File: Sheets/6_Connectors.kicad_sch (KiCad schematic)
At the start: 2 parts, among them J4 Conn_02x26_Odd_Even, J5 Conn_02x26_Odd_Even

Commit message: Updates for revision 2
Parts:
- J4, J5: MANUFACTURER (none) -> HRS(Hirose); MAXIMUM_PACKAGE_HEIGHT HRS(Hirose) -> (none)
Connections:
- net VCC is gone; now on net +3V3: J4.51 (Pin_51), J4.52 (Pin_52)
- net P1.09 renamed P1.09/~{CHARGE}

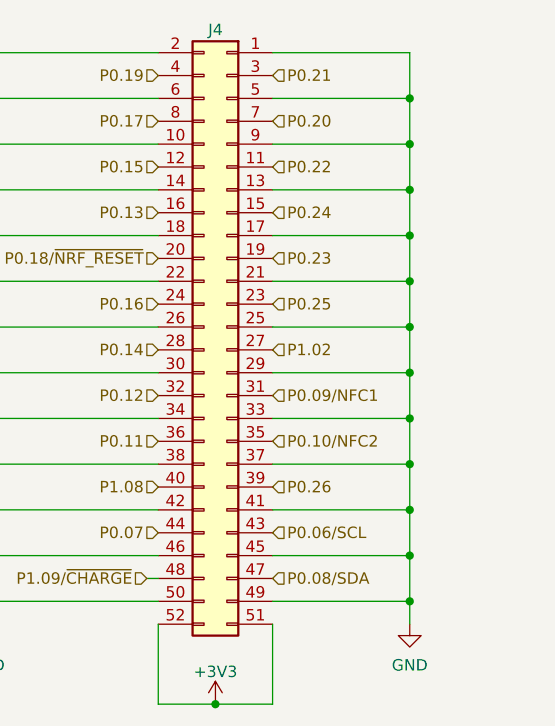
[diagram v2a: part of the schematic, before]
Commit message: Moving some tracks and increasing via diameter to allow for latest JLCPCB capabilities
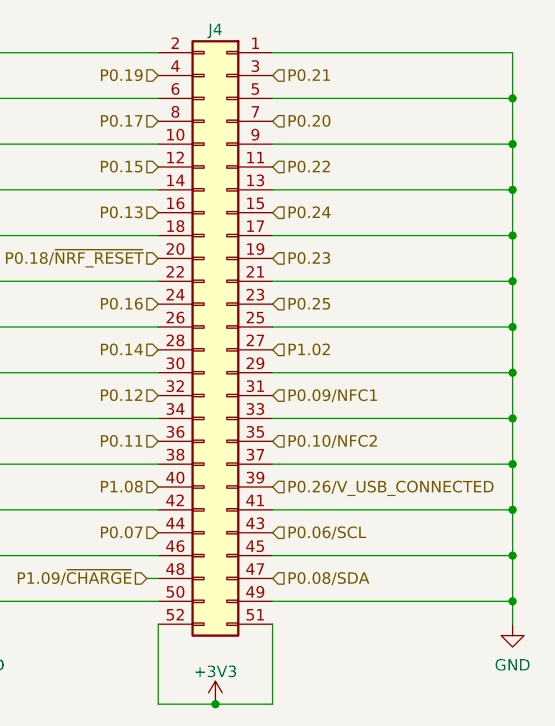
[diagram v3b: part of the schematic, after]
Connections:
- net P0.26 renamed P0.26/V_USB_CONNECTED
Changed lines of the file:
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@@
   (junction (at 158.75 64.77) (diameter 0) (color 0 0 0 0)
   )
-  (junction (at 205.74 59.69) (diameter 0) (color 0 0 0 0)
+  (junction (at 217.17 59.69) (diameter 0) (color 0 0 0 0)
   )
   (junction (at 72.39 71.12) (diameter 0) (color 0 0 0 0)
@@
   (junction (at 158.75 85.09) (diameter 0) (color 0 0 0 0)
   )
-  (junction (at 205.74 85.09) (diameter 0) (color 0 0 0 0)
-  )
-  (junction (at 205.74 100.33) (diameter 0) (color 0 0 0 0)
+  (junction (at 217.17 85.09) (diameter 0) (color 0 0 0 0)
   )
   (junction (at 113.03 88.9) (diameter 0) (color 0 0 0 0)
@@
   (junction (at 158.75 59.69) (diameter 0) (color 0 0 0 0)
   )
-  (junction (at 205.74 110.49) (diameter 0) (color 0 0 0 0)
+  (junction (at 217.17 110.49) (diameter 0) (color 0 0 0 0)
   )
   (junction (at 72.39 81.28) (diameter 0) (color 0 0 0 0)
@@
   (junction (at 113.03 101.6) (diameter 0) (color 0 0 0 0)
   )
-  (junction (at 205.74 74.93) (diameter 0) (color 0 0 0 0)
+  (junction (at 217.17 74.93) (diameter 0) (color 0 0 0 0)
   )
   (junction (at 113.03 96.52) (diameter 0) (color 0 0 0 0)
   )
+  (junction (at 217.17 100.33) (diameter 0) (color 0 0 0 0)
+  )
   (junction (at 113.03 60.96) (diameter 0) (color 0 0 0 0)
   )
@@
   (junction (at 113.03 116.84) (diameter 0) (color 0 0 0 0)
   )
+  (junction (at 217.17 105.41) (diameter 0) (color 0 0 0 0)
+  )
   (junction (at 184.15 127) (diameter 0) (color 0 0 0 0)
   )
   (junction (at 158.75 100.33) (diameter 0) (color 0 0 0 0)
   )
-  (junction (at 205.74 64.77) (diameter 0) (color 0 0 0 0)
+  (junction (at 217.17 64.77) (diameter 0) (color 0 0 0 0)
   )
   (junction (at 158.75 105.41) (diameter 0) (color 0 0 0 0)
@@
   (junction (at 113.03 81.28) (diameter 0) (color 0 0 0 0)
   )
-  (junction (at 205.74 105.41) (diameter 0) (color 0 0 0 0)
-  )
   (junction (at 113.03 76.2) (diameter 0) (color 0 0 0 0)
   )
@@
   (junction (at 72.39 111.76) (diameter 0) (color 0 0 0 0)
   )
-  (junction (at 205.74 95.25) (diameter 0) (color 0 0 0 0)
+  (junction (at 217.17 95.25) (diameter 0) (color 0 0 0 0)
   )
   (junction (at 72.39 76.2) (diameter 0) (color 0 0 0 0)
@@
   (junction (at 72.39 86.36) (diameter 0) (color 0 0 0 0)
   )
-  (junction (at 205.74 69.85) (diameter 0) (color 0 0 0 0)
-  )
-  (junction (at 205.74 90.17) (diameter 0) (color 0 0 0 0)
+  (junction (at 217.17 69.85) (diameter 0) (color 0 0 0 0)
+  )
+  (junction (at 217.17 90.17) (diameter 0) (color 0 0 0 0)
   )
   (junction (at 158.75 74.93) (diameter 0) (color 0 0 0 0)
@@
   (junction (at 113.03 66.04) (diameter 0) (color 0 0 0 0)
   )
-  (junction (at 205.74 80.01) (diameter 0) (color 0 0 0 0)
+  (junction (at 217.17 80.01) (diameter 0) (color 0 0 0 0)
   )
   (junction (at 113.03 111.76) (diameter 0) (color 0 0 0 0)
@@
   (junction (at 72.39 96.52) (diameter 0) (color 0 0 0 0)
   )
-  (junction (at 205.74 115.57) (diameter 0) (color 0 0 0 0)
+  (junction (at 217.17 115.57) (diameter 0) (color 0 0 0 0)
   )
   (wire (pts (xy 158.75 100.33) (xy 158.75 105.41))
@@
     (stroke (width 0) (type default))
   )
-  (wire (pts (xy 205.74 69.85) (xy 205.74 74.93))
+  (wire (pts (xy 217.17 69.85) (xy 217.17 74.93))
     (stroke (width 0) (type default))
   )
@@
     (stroke (width 0) (type default))
   )
-  (wire (pts (xy 190.5 69.85) (xy 205.74 69.85))
+  (wire (pts (xy 190.5 69.85) (xy 217.17 69.85))
     (stroke (width 0) (type default))
   )
@@
     (stroke (width 0) (type default))
   )
-  (wire (pts (xy 190.5 80.01) (xy 205.74 80.01))
+  (wire (pts (xy 190.5 80.01) (xy 217.17 80.01))
     (stroke (width 0) (type default))
   )
@@
     (stroke (width 0) (type default))
   )
+  (wire (pts (xy 190.5 110.49) (xy 217.17 110.49))
+    (stroke (width 0) (type default))
+  )
   (wire (pts (xy 158.75 105.41) (xy 177.8 105.41))
     (stroke (width 0) (type default))
@@
     (stroke (width 0) (type default))
   )
-  (wire (pts (xy 205.74 90.17) (xy 190.5 90.17))
-    (stroke (width 0) (type default))
-  )
-  (wire (pts (xy 205.74 64.77) (xy 205.74 69.85))
+  (wire (pts (xy 217.17 90.17) (xy 190.5 90.17))
+    (stroke (width 0) (type default))
+  )
+  (wire (pts (xy 217.17 64.77) (xy 217.17 69.85))
     (stroke (width 0) (type default))
   )
@@
     (stroke (width 0) (type default))
   )
-  (wire (pts (xy 190.5 74.93) (xy 205.74 74.93))
+  (wire (pts (xy 190.5 74.93) (xy 217.17 74.93))
     (stroke (width 0) (type default))
   )
@@
     (stroke (width 0) (type default))
   )
+  (wire (pts (xy 190.5 100.33) (xy 217.17 100.33))
+    (stroke (width 0) (type default))
+  )
   (wire (pts (xy 99.06 96.52) (xy 113.03 96.52))
     (stroke (width 0) (type default))
@@
     (stroke (width 0) (type default))
   )
-  (wire (pts (xy 205.74 105.41) (xy 205.74 110.49))
+  (wire (pts (xy 217.17 105.41) (xy 217.17 110.49))
     (stroke (width 0) (type default))
   )
@@
     (stroke (width 0) (type default))
   )
-  (wire (pts (xy 205.74 74.93) (xy 205.74 80.01))
-    (stroke (width 0) (type default))
-  )
-  (wire (pts (xy 190.5 100.33) (xy 205.74 100.33))
+  (wire (pts (xy 217.17 74.93) (xy 217.17 80.01))
     (stroke (width 0) (type default))
   )
@@
     (stroke (width 0) (type default))
   )
-  (wire (pts (xy 205.74 90.17) (xy 205.74 95.25))
+  (wire (pts (xy 217.17 90.17) (xy 217.17 95.25))
     (stroke (width 0) (type default))
   )
@@
     (stroke (width 0) (type default))
   )
-  (wire (pts (xy 190.5 110.49) (xy 205.74 110.49))
-    (stroke (width 0) (type default))
-  )
-  (wire (pts (xy 190.5 54.61) (xy 205.74 54.61))
+  (wire (pts (xy 190.5 54.61) (xy 217.17 54.61))
     (stroke (width 0) (type default))
   )
@@
     (stroke (width 0) (type default))
   )
-  (wire (pts (xy 190.5 59.69) (xy 205.74 59.69))
+  (wire (pts (xy 190.5 59.69) (xy 217.17 59.69))
     (stroke (width 0) (type default))
   )
@@
     (stroke (width 0) (type default))
   )
-  (wire (pts (xy 205.74 54.61) (xy 205.74 59.69))
-    (stroke (width 0) (type default))
-  )
-  (wire (pts (xy 205.74 110.49) (xy 205.74 115.57))
+  (wire (pts (xy 217.17 54.61) (xy 217.17 59.69))
+    (stroke (width 0) (type default))
+  )
+  (wire (pts (xy 217.17 110.49) (xy 217.17 115.57))
     (stroke (width 0) (type default))
   )
@@
     (stroke (width 0) (type default))
   )
-  (wire (pts (xy 205.74 80.01) (xy 205.74 85.09))
+  (wire (pts (xy 217.17 80.01) (xy 217.17 85.09))
     (stroke (width 0) (type default))
   )
@@
     (stroke (width 0) (type default))
   )
-  (wire (pts (xy 205.74 85.09) (xy 205.74 90.17))
+  (wire (pts (xy 217.17 85.09) (xy 217.17 90.17))
     (stroke (width 0) (type default))
   )
@@
     (stroke (width 0) (type default))
   )
-  (wire (pts (xy 190.5 64.77) (xy 205.74 64.77))
+  (wire (pts (xy 190.5 64.77) (xy 217.17 64.77))
     (stroke (width 0) (type default))
   )
@@
     (stroke (width 0) (type default))
   )
-  (wire (pts (xy 205.74 59.69) (xy 205.74 64.77))
+  (wire (pts (xy 217.17 59.69) (xy 217.17 64.77))
     (stroke (width 0) (type default))
   )
@@
     (stroke (width 0) (type default))
   )
-  (wire (pts (xy 205.74 95.25) (xy 205.74 100.33))
+  (wire (pts (xy 217.17 95.25) (xy 217.17 100.33))
     (stroke (width 0) (type default))
   )
@@
     (stroke (width 0) (type default))
   )
-  (wire (pts (xy 205.74 100.33) (xy 205.74 105.41))
+  (wire (pts (xy 217.17 100.33) (xy 217.17 105.41))
     (stroke (width 0) (type default))
   )
@@
     (stroke (width 0) (type default))
   )
-  (wire (pts (xy 190.5 95.25) (xy 205.74 95.25))
+  (wire (pts (xy 190.5 95.25) (xy 217.17 95.25))
     (stroke (width 0) (type default))
   )
@@
     (stroke (width 0) (type default))
   )
-  (wire (pts (xy 205.74 115.57) (xy 205.74 118.11))
+  (wire (pts (xy 217.17 115.57) (xy 217.17 118.11))
     (stroke (width 0) (type default))
   )
@@
     (stroke (width 0) (type default))
   )
-  (wire (pts (xy 190.5 85.09) (xy 205.74 85.09))
+  (wire (pts (xy 190.5 85.09) (xy 217.17 85.09))
     (stroke (width 0) (type default))
   )
@@
     (stroke (width 0) (type default))
   )
-  (wire (pts (xy 190.5 105.41) (xy 205.74 105.41))
-    (stroke (width 0) (type default))
-  )
-  (wire (pts (xy 190.5 115.57) (xy 205.74 115.57))
+  (wire (pts (xy 190.5 105.41) (xy 217.17 105.41))
+    (stroke (width 0) (type default))
+  )
+  (wire (pts (xy 190.5 115.57) (xy 217.17 115.57))
     (stroke (width 0) (type default))
   )
@@
     (effects (font (size 1.27 1.27)) (justify right))
   )
-  (hierarchical_label "P0.26" (shape input) (at 190.5 102.87 0) (fields_autoplaced)
+  (hierarchical_label "P0.26{slash}V_USB_CONNECTED" (shape input) (at 190.5 102.87 0) (fields_autoplaced)
     (effects (font (size 1.27 1.27)) (justify left))
   )
@@
     (effects (font (size 1.27 1.27)) (justify right))
   )
-  (symbol (lib_id "power:GND") (at 205.74 118.11 0) (unit 1)
+  (symbol (lib_id "power:GND") (at 217.17 118.11 0) (unit 1)
     (in_bom yes) (on_board yes) (dnp no) (fields_autoplaced)
-    (property "Reference" "#PWR0106" (at 205.74 124.46 0)
+    (property "Reference" "#PWR0106" (at 217.17 124.46 0)
       (effects (font (size 1.27 1.27)) hide)
     )
-    (property "Value" "GND" (at 205.74 122.6725 0)
+    (property "Value" "GND" (at 217.17 122.6725 0)
       (effects (font (size 1.27 1.27)))
     )
-    (property "Footprint" "" (at 205.74 118.11 0)
+    (property "Footprint" "" (at 217.17 118.11 0)
       (effects (font (size 1.27 1.27)) hide)
     )
-    (property "Datasheet" "" (at 205.74 118.11 0)
+    (property "Datasheet" "" (at 217.17 118.11 0)
       (effects (font (size 1.27 1.27)) hide)
     )

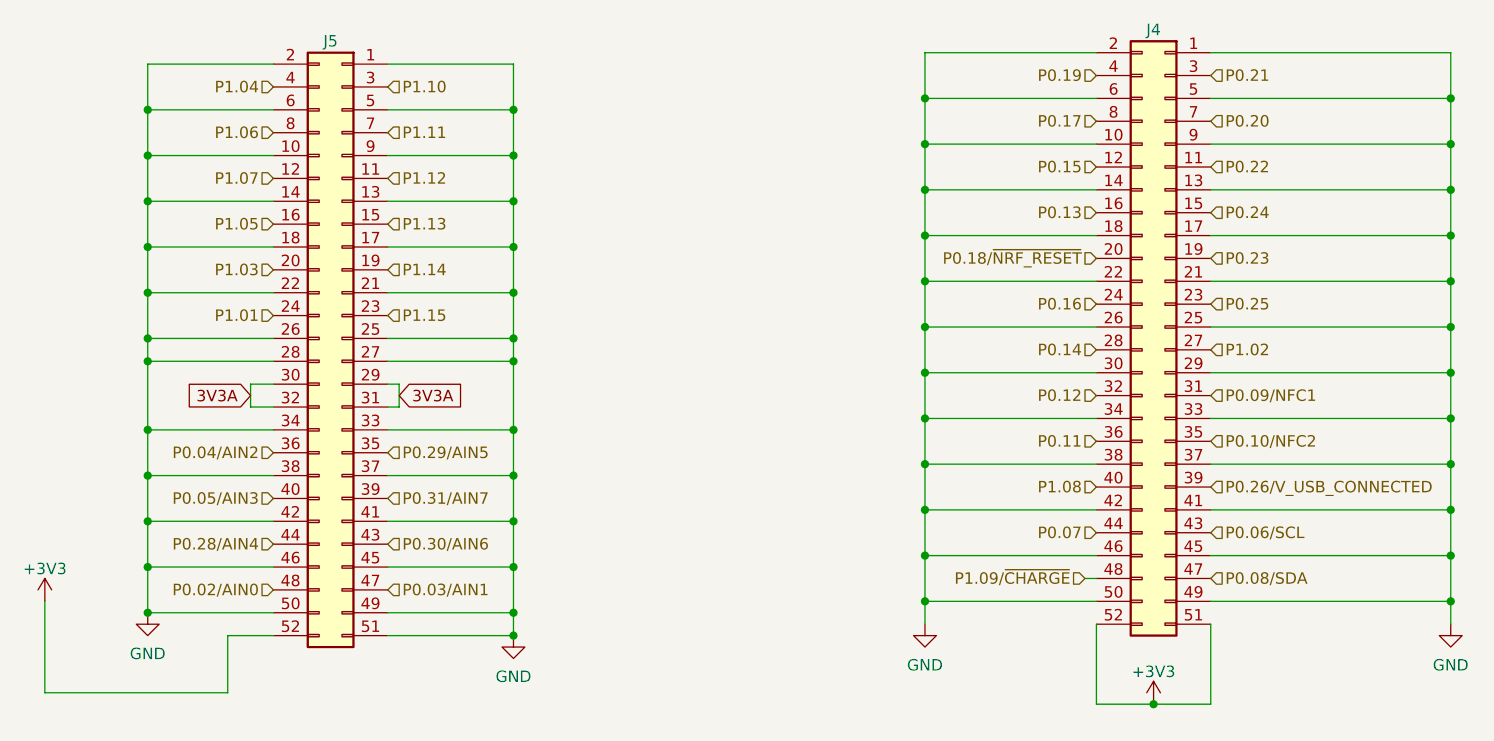
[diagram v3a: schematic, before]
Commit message: changed LED net names to indicate status LEDs and changed 3V3 pin on mezzanine connector to be GND
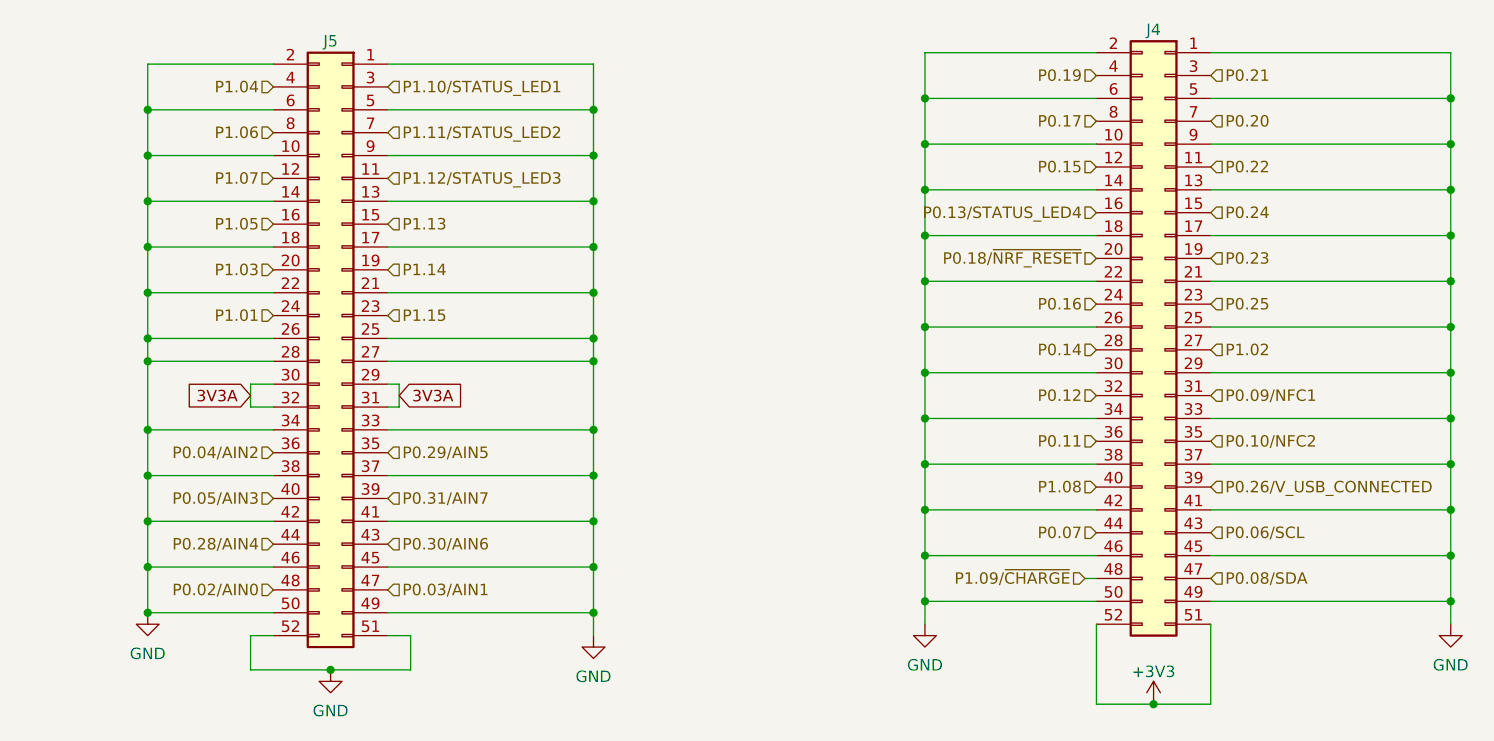
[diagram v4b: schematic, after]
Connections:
- net +3V3: no longer J5.52 (Pin_52)
- net GND: now also J5.52 (Pin_52)
- net P0.13 renamed P0.13/STATUS_LED4
- net P1.10 renamed P1.10/STATUS_LED1
- net P1.11 renamed P1.11/STATUS_LED2
- net P1.12 renamed P1.12/STATUS_LED3
